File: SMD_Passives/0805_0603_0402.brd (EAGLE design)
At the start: 10.4 x 3.5 mm, 5 parts

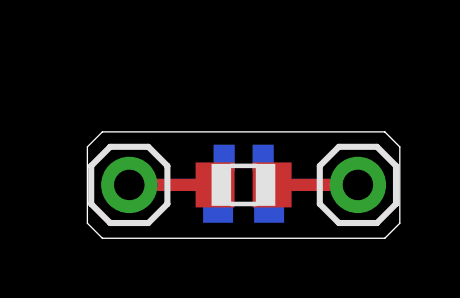
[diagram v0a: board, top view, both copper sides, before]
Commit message: Updated passive SMD breakout boards to meet PCB specs
JLC PCB requires a 5x5mm minimum size, and the single SMD adapters were too small for this, so converted to make them wide enough, and made them "dual" to maximize the spaced used
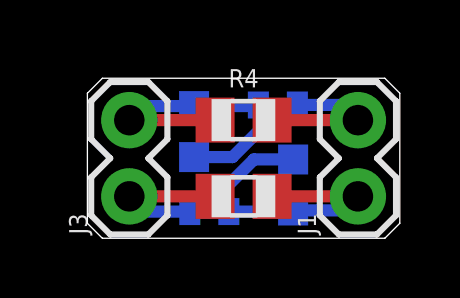
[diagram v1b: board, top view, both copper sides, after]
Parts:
- removed J2: (no value), bschulz:1X01
- added J3: (no value), bschulz:1X02
- added R4: (no value), bschulz_passives:R0805
- added R5: (no value), bschulz_passives:R0603
- added R6: (no value), bschulz_passives:R0402
- J1: device bschulz:1X01 -> bschulz:1X02
- moved J1 7.63 mm to (9.02, 1.40), turned to 90 degrees
- moved R3 2.11 mm to (4.06, 0.89)
- moved R2 1.82 mm to (6.86, 1.78), turned to 270 degrees
- moved R1 0.38 mm to (5.21, 1.40)
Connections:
- removed net N$1: J1.1, R1.1, R2.1, R3.1
- removed net N$2: J2.1, R1.2, R2.2, R3.2
- new net R1_A: J3.1, R1.1, R2.1, R3.1
- new net R1_B: J1.1, R1.2, R2.2, R3.2
- new net R2_A: J3.2, R4.1, R5.1, R6.1
- new net R2_B: J1.2, R4.2, R5.2, R6.2
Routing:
- net R1_A: track 0.00 -> 9.32 mm
- net R2_B: track 0.00 -> 9.25 mm
- net N$1: track 7.75 -> 0.00 mm
- net N$2: track 7.75 -> 0.00 mm
- net R2_A: track 0.00 -> 7.37 mm
- net R1_B: track 0.00 -> 7.37 mm
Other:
- board size 10.4 x 3.5 mm -> 10.4 x 5.3 mm
